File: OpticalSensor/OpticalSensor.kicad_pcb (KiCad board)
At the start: 2 copper layers, 30 x 20.5 mm, 6 parts, among them J1 Conn_01x03, U1 EE_SX1103

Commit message: Initial board
Added complementary components
Board should be functional
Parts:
- added D1: BAT54KFILM, Diode_SMD:D_SOD-523, F.Cu at (158.8, 94.5)
- added Q1: T2N7002AK, Package_TO_SOT_SMD:SOT-23, F.Cu at (147.6, 92.0)
- added R1: 330R, Resistor_SMD:R_0402_1005Metric, F.Cu at (153.5, 96.5)
- added R2: 10K, Resistor_SMD:R_0402_1005Metric, F.Cu at (160.0, 90.0)
- added R3: 56K, Resistor_SMD:R_0402_1005Metric, F.Cu at (160.0, 92.5)
- added R4: 10K, Resistor_SMD:R_0402_1005Metric, F.Cu at (148.5, 96.5)
- added REF**: OSHW-Symbol_6.7x6mm_SilkScreen, Symbol:OSHW-Symbol_6.7x6mm_SilkScreen, B.Cu at (144.5, 93.5)
- J1: value Conn_01x03 -> Conn_01x03_MountingPin
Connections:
- J1 pad 1: unconnected-(J1-Pin_1-Pad1) -> Net-(D1-K)
- J1 pad 2: unconnected-(J1-Pin_2-Pad2) -> VCC
- J1 pad 3: unconnected-(J1-Pin_3-Pad3) -> /OUT
- J1 pad MP: (no net) -> unconnected-(J1-MountPin-PadMP)
- U1 pad 1: unconnected-(U1-Pad1) -> Net-(R1-Pad2)
- U1 pad 2: unconnected-(U1-Pad2) -> GND
- U1 pad 3: unconnected-(U1-Pad3) -> GND
- U1 pad 4: unconnected-(U1-Pad4) -> Net-(Q1-G)
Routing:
- net VCC: track 0.00 -> 27.5 mm
- net /OUT: track 0.00 -> 19.2 mm
- net Net-(Q1-G): track 0.00 -> 14.5 mm
- net Net-(D1-K): track 0.00 -> 5.90 mm
- net Net-(R1-Pad2): track 0.00 -> 2.85 mm
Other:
- board text added: "5"
- board text added: "G"
- board text added: "S"

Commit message: Power and status led
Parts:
- added D2: LED_Dual_AKAK, easyeda2kicad:LED-ARRAY-SMD_4P-L1.6-W1.3-BR-FD, F.Cu at (142.8, 93.6)
- added R5: 120R, Resistor_SMD:R_0402_1005Metric, F.Cu at (146.5, 94.5)
- added R6: 120R, Resistor_SMD:R_0402_1005Metric, F.Cu at (144.0, 91.5)
- moved R4 2.05 mm to (149.0, 94.5), turned to 0 degrees
- moved H1 1.00 mm to (146.0, 102.5)
- moved H2 1.00 mm to (162.0, 102.5)
- moved G*** 0.50 mm to (154.0, 101.0) (x2)
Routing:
- net VCC: track 27.5 -> 44.6 mm
- net Net-(D2-A1): track 0.00 -> 2.70 mm
- net Net-(D2-A2): track 0.00 -> 1.66 mm
- net GND: vias 0 -> 8
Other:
- board size 30 x 20.5 mm -> 30 x 21.5 mm
- board text added: "V1.0"

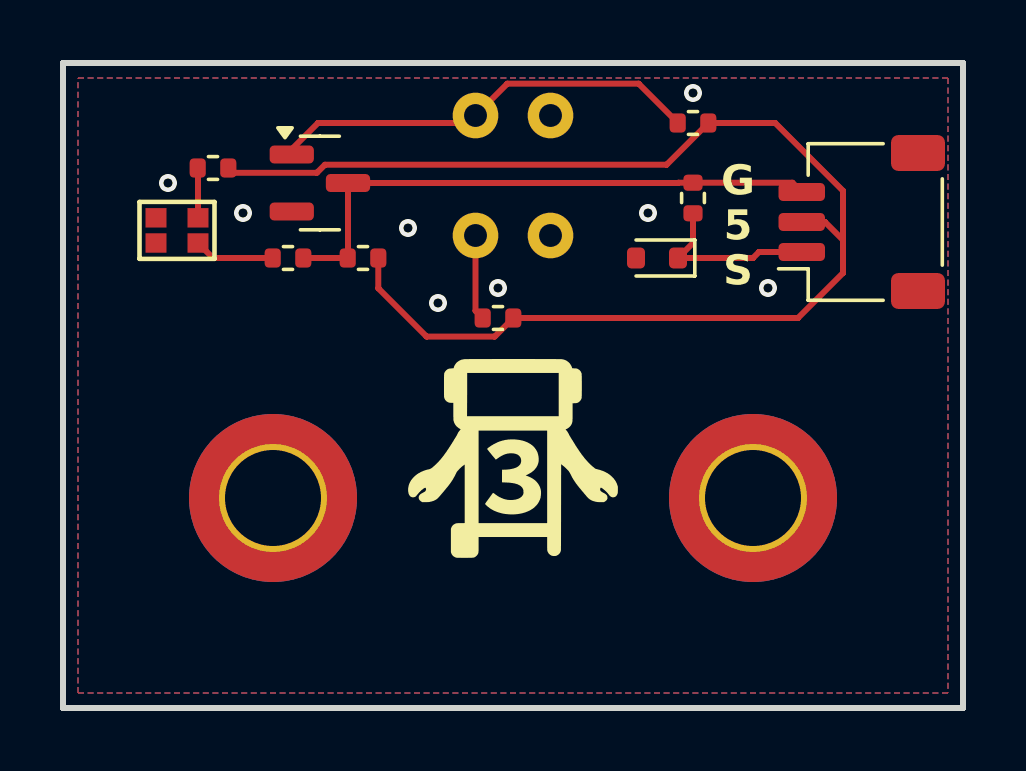
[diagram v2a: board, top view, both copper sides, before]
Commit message: LCSC component part numbers, board resize
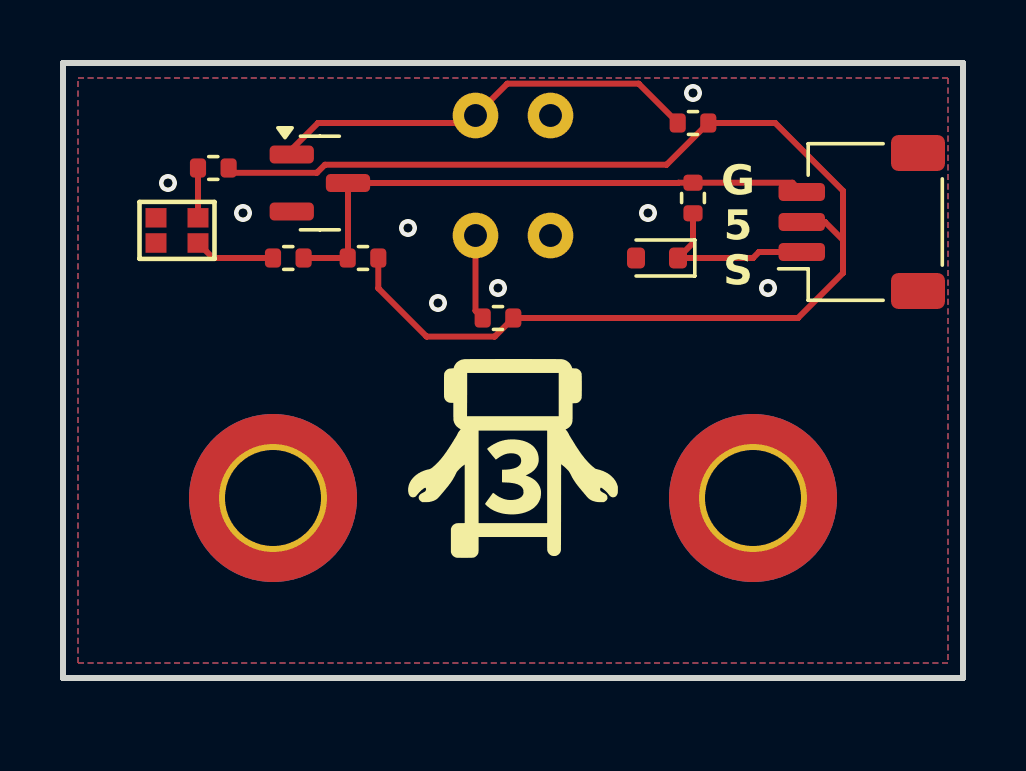
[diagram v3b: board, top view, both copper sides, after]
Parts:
- R6: value 120R -> 200R
- moved R6 3.91 mm to (146.5, 94.5)
- moved R5 3.90 mm to (144.0, 91.5)
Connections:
- R5 pad 1: /OUT -> VCC
- R5 pad 2: Net-(D2-A1) -> Net-(D2-A2)
- R6 pad 1: VCC -> /OUT
- R6 pad 2: Net-(D2-A2) -> Net-(D2-A1)
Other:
- board size 30 x 21.5 mm -> 30 x 20.5 mm
- board text added: "Kevinbot Optical Switch"
- board text removed: "Kevinbot Optical Sensor"

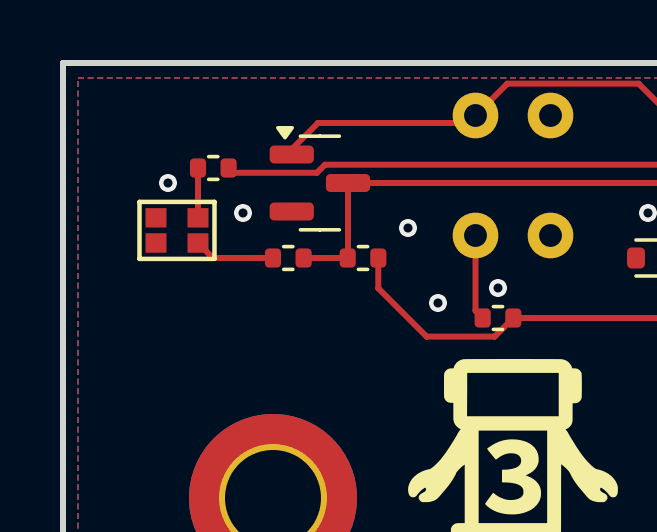
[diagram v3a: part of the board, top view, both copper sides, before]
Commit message: Led footprint updates
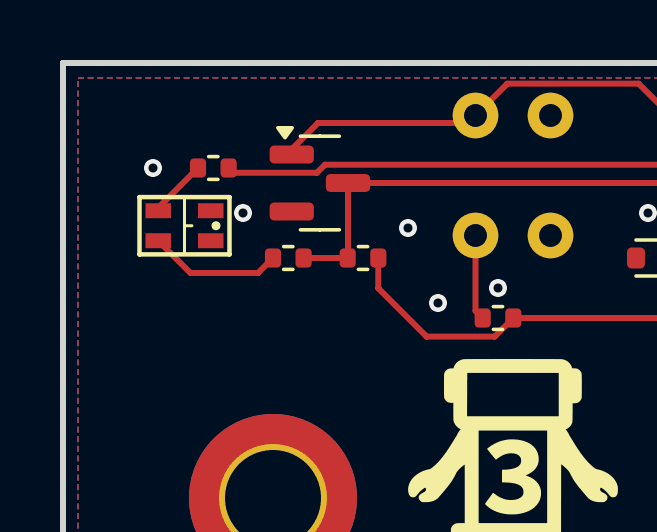
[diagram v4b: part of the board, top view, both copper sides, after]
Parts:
- D2: footprint easyeda2kicad:LED-ARRAY-SMD_4P-L1.6-W1.3-BR-FD -> Lighting:QBLP600-RIB
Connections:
- R5 pad 1: VCC -> /OUT
- R5 pad 2: Net-(D2-A2) -> Net-(D2-A1)
- R6 pad 1: /OUT -> VCC
- R6 pad 2: Net-(D2-A1) -> Net-(D2-A2)
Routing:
- net Net-(D2-A2): track 1.66 -> 4.48 mm
- net Net-(D2-A1): track 2.70 -> 1.99 mm

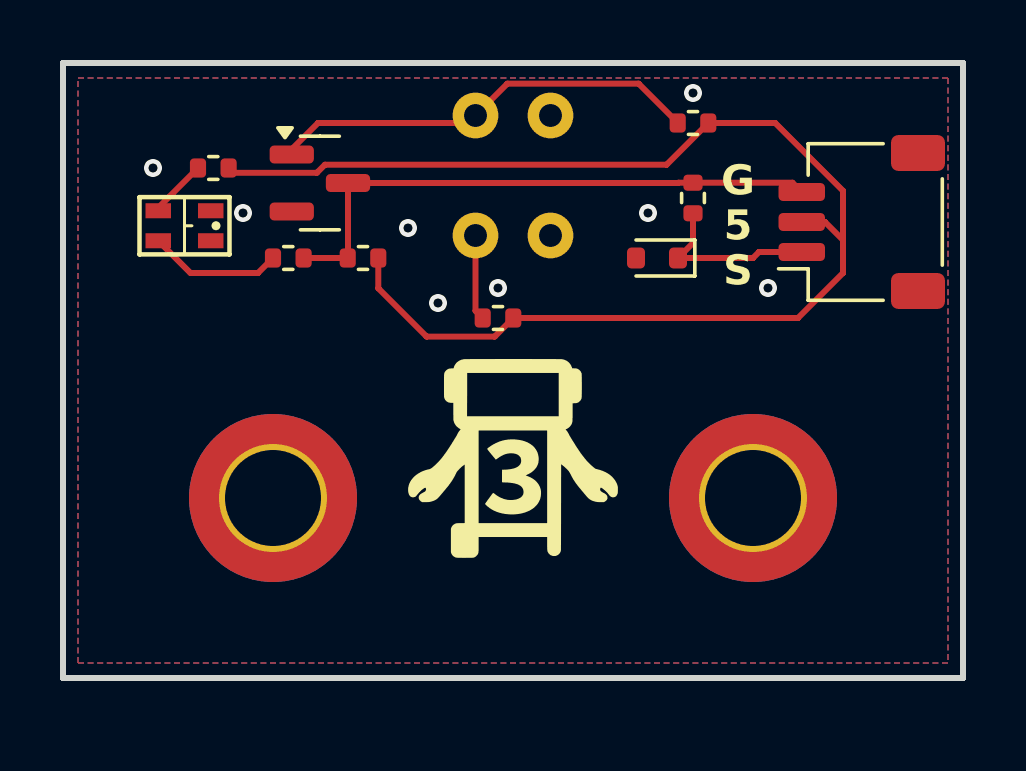
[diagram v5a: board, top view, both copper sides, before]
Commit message: fix optical sensor routing
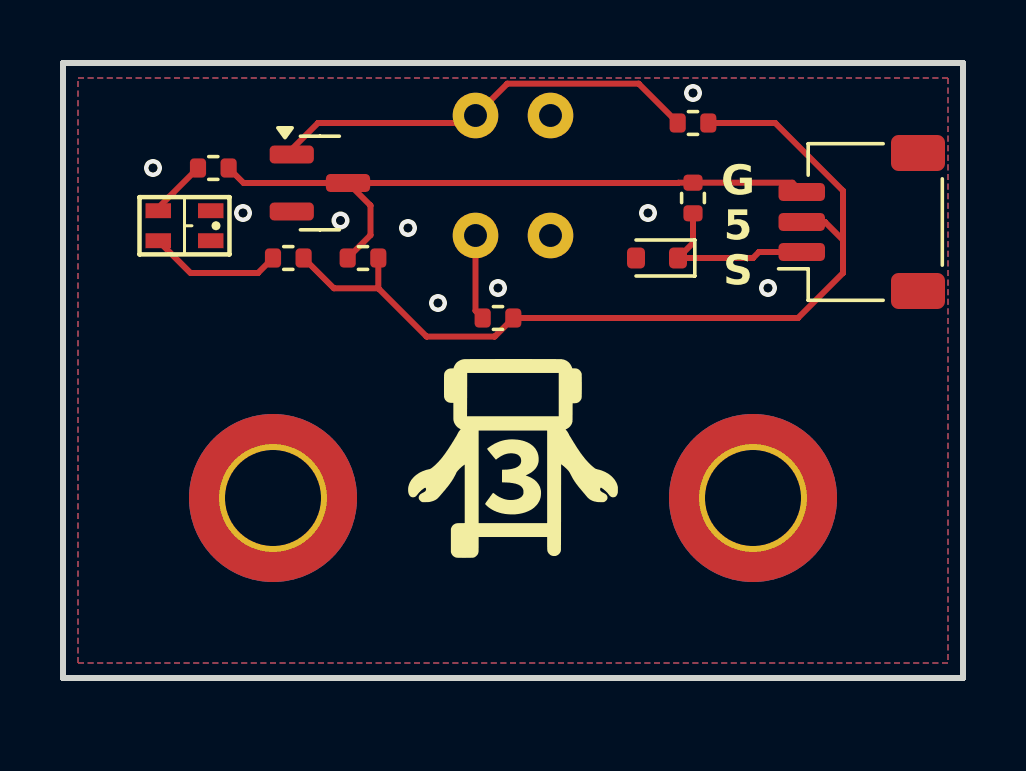
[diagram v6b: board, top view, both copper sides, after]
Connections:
- J1 pad MP: unconnected-(J1-MountPin-PadMP) -> GND
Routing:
- net VCC: track 44.6 -> 30.7 mm
- net /OUT: track 19.2 -> 22.6 mm
- net GND: vias 8 -> 9
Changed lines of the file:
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@@
 	(net 5 "Net-(Q1-G)")
 	(net 6 "Net-(R1-Pad2)")
-	(net 7 "unconnected-(J1-MountPin-PadMP)")
-	(net 8 "Net-(D2-A1)")
-	(net 9 "Net-(D2-A2)")
+	(net 7 "Net-(D2-A1)")
+	(net 8 "Net-(D2-A2)")
 	(footprint "Connector_JST:JST_SH_SM03B-SRSS-TB_1x03-1MP_P1.00mm_Horizontal"
 		(layer "F.Cu")
@@
 			(layers "F.Cu" "F.Paste" "F.Mask")
 			(roundrect_rratio 0.208333)
-			(net 7 "unconnected-(J1-MountPin-PadMP)")
+			(net 1 "GND")
 			(pinfunction "MountPin")
 			(pintype "passive")
@@
 			(layers "F.Cu" "F.Paste" "F.Mask")
 			(roundrect_rratio 0.208333)
-			(net 7 "unconnected-(J1-MountPin-PadMP)")
+			(net 1 "GND")
 			(pinfunction "MountPin")
 			(pintype "passive")
@@
 			(layers "F.Cu" "F.Paste" "F.Mask")
 			(roundrect_rratio 0.25)
-			(net 9 "Net-(D2-A2)")
+			(net 8 "Net-(D2-A2)")
 			(pintype "passive")
 		)
@@
 			(layers "F.Cu" "F.Paste" "F.Mask")
 			(roundrect_rratio 0.25)
-			(net 8 "Net-(D2-A1)")
+			(net 7 "Net-(D2-A1)")
 			(pintype "passive")
 		)
@@
 			(size 0.85 0.5)
 			(layers "F.Cu" "F.Paste" "F.Mask")
-			(net 8 "Net-(D2-A1)")
+			(net 7 "Net-(D2-A1)")
 			(pinfunction "A1")
 			(pintype "input")
@@
 			(size 0.85 0.5)
 			(layers "F.Cu" "F.Paste" "F.Mask")
-			(net 9 "Net-(D2-A2)")
+			(net 8 "Net-(D2-A2)")
 			(pinfunction "A2")
 			(pintype "input")
@@
 			(effects
 				(font
-					(size 0.5 0.5)
+					(size 0.8 0.8)
 					(thickness 0.125)
 				)
@@
 	)
 	(via
+		(at 148.25 93.25)
+		(size 0.6)
+		(drill 0.3)
+		(layers "F.Cu" "B.Cu")
+		(free yes)
+		(net 1)
+	)
+	(via
 		(at 158.5 93)
 		(size 0.6)
@@
 	)
 	(segment
-		(start 159.119448 91.390552)
-		(end 160.51 90)
+		(start 147.02 94.5)
+		(end 148.03 95.51)
 		(width 0.2)
 		(layer "F.Cu")
@@
 	)
 	(segment
-		(start 144.669448 91.659448)
-		(end 147.4625 91.659448)
-		(width 0.2)
-		(layer "F.Cu")
-		(net 3)
-	)
-	(segment
-		(start 147.4625 91.659448)
-		(end 147.731396 91.390552)
-		(width 0.2)
-		(layer "F.Cu")
-		(net 3)
-	)
-	(segment
 		(start 160.51 90)
 		(end 162.740552 90)
@@
 	)
 	(segment
-		(start 144.51 91.5)
-		(end 144.669448 91.659448)
+		(start 148.03 95.51)
+		(end 149.51 95.51)
 		(width 0.2)
 		(layer "F.Cu")
@@
 	)
 	(segment
-		(start 147.731396 91.390552)
-		(end 159.119448 91.390552)
+		(start 149.51 95.51)
+		(end 149.51 94.5)
 		(width 0.2)
 		(layer "F.Cu")
@@
 	)
 	(segment
-		(start 149.51 95.51)
-		(end 149.51 94.5)
+		(start 159.5 92)
+		(end 148.5 92)
 		(width 0.2)
 		(layer "F.Cu")
-		(net 3)
+		(net 4)
 	)
 	(segment
-		(start 148.49 94.5)
-		(end 148.5 94.49)
+		(start 149.25 92.75)
+		(end 148.5 92)
 		(width 0.2)
 		(layer "F.Cu")
@@
 	)
 	(segment
-		(start 159.5 92)
-		(end 148.5 92)
+		(start 163.315 91.99)
+		(end 163.625 92.3)
 		(width 0.2)
 		(layer "F.Cu")
@@
 	)
 	(segment
-		(start 147.01 94.5)
-		(end 148.49 94.5)
+		(start 148.5 92)
+		(end 145.02 92)
 		(width 0.2)
 		(layer "F.Cu")
@@
 	)
 	(segment
-		(start 163.315 91.99)
-		(end 163.625 92.3)
+		(start 145.02 92)
+		(end 144.52 91.5)
 		(width 0.2)
 		(layer "F.Cu")
@@
 	)
 	(segment
-		(start 148.5 94.49)
-		(end 148.5 92)
+		(start 148.49 94.5)
+		(end 149.25 93.74)
 		(width 0.2)
 		(layer "F.Cu")
@@
 	)
 	(segment
+		(start 149.25 93.74)
+		(end 149.25 92.75)
+		(width 0.2)
+		(layer "F.Cu")
+		(net 4)
+	)
+	(segment
 		(start 160 91.99)
 		(end 159.51 91.99)
@@
 		(width 0.2)
 		(layer "F.Cu")
-		(net 8)
+		(net 7)
 	)
 	(segment
@@
 		(width 0.2)
 		(layer "F.Cu")
-		(net 8)
+		(net 7)
 	)
 	(segment
@@
 		(width 0.2)
 		(layer "F.Cu")
-		(net 8)
+		(net 7)
 	)
 	(segment
@@
 		(width 0.2)
 		(layer "F.Cu")
-		(net 9)
+		(net 8)
 	)
 	(segment
@@
 		(width 0.2)
 		(layer "F.Cu")
-		(net 9)
+		(net 8)
 	)
 	(segment
@@
 		(width 0.2)
 		(layer "F.Cu")
-		(net 9)
+		(net 8)
 	)
 	(zone
